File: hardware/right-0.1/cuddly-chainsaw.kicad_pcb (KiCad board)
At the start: 2 copper layers, 181.9 x 100.8 mm, 145 parts, among them J1 USB_C_Receptacle_USB2.0, J2 USB_C_Receptacle_USB2.0, J3 AVR-ISP-6, SW1 Encoder_MX_RGB, SW10 MX_RGB, SW11 MX_RGB, SW12 MX_RGB, SW13 MX_RGB, SW14 MX_RGB, SW15 MX_RGB, SW16 MX_RGB, SW17 MX_RGB, SW18 MX_RGB, SW19 MX_RGB, SW2 MX_RGB, SW20 MX_RGB, SW21 MX_RGB, SW22 MX_RGB, SW23 MX_RGB, SW24 MX_RGB, SW25 MX_RGB, SW26 MX_RGB, SW27 MX_RGB, SW28 MX_RGB, SW29 MX_RGB, SW3 MX_RGB, SW30 MX_RGB, SW31 MX_RGB, SW32 MX_RGB, SW33 MX_RGB, SW34 MX_RGB, SW35 SW_Push, SW36 MX_RGB, SW37 MX_RGB, SW38 MX_RGB, SW39 MX_RGB, SW4 MX_RGB, SW40 MX_RGB, SW41 MX_RGB, SW42 MX_RGB, SW5 MX_RGB, SW6 MX_RGB, SW7 MX_RGB, SW8 MX_RGB, SW9 MX_RGB, U1 USBLC6-2SC6, U2 ATmega32U4-MU, Y1 16MHz

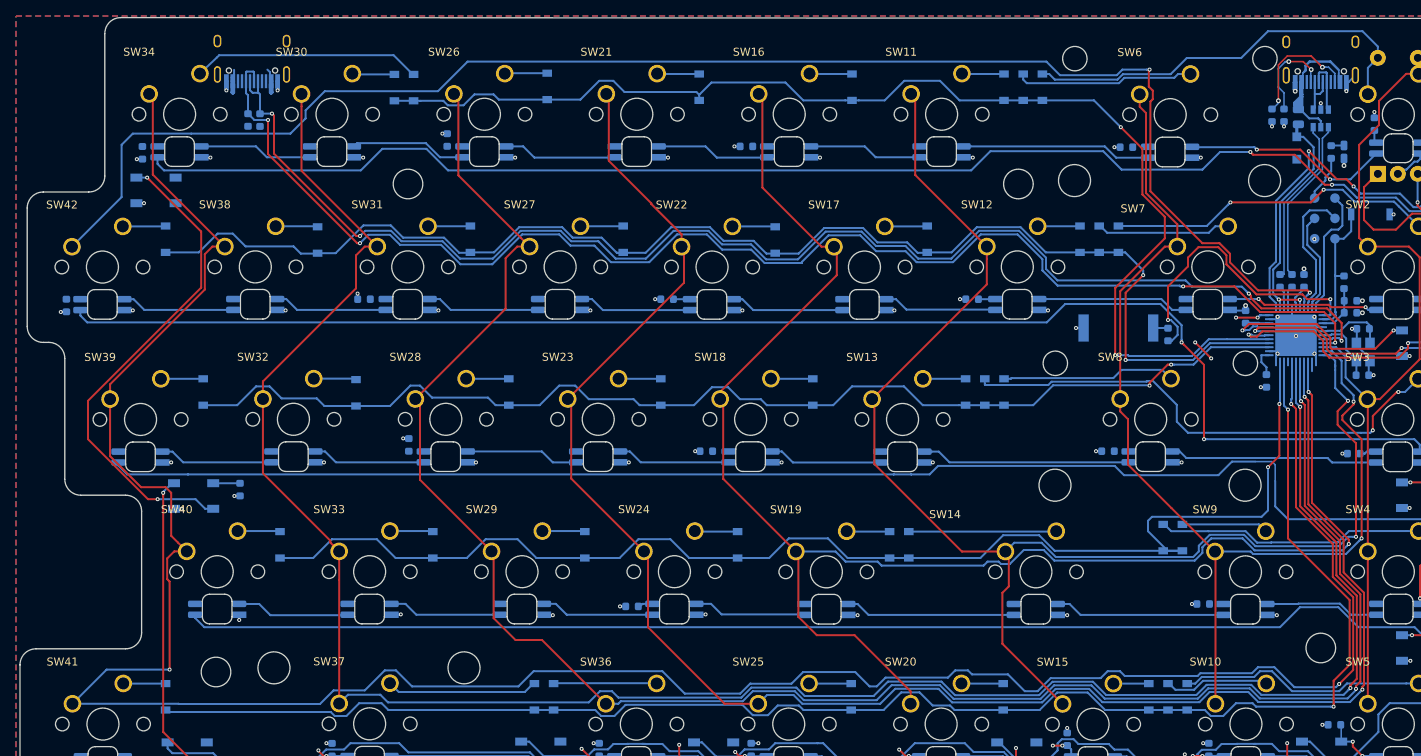
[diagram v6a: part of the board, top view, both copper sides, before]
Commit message: update board with new footprints
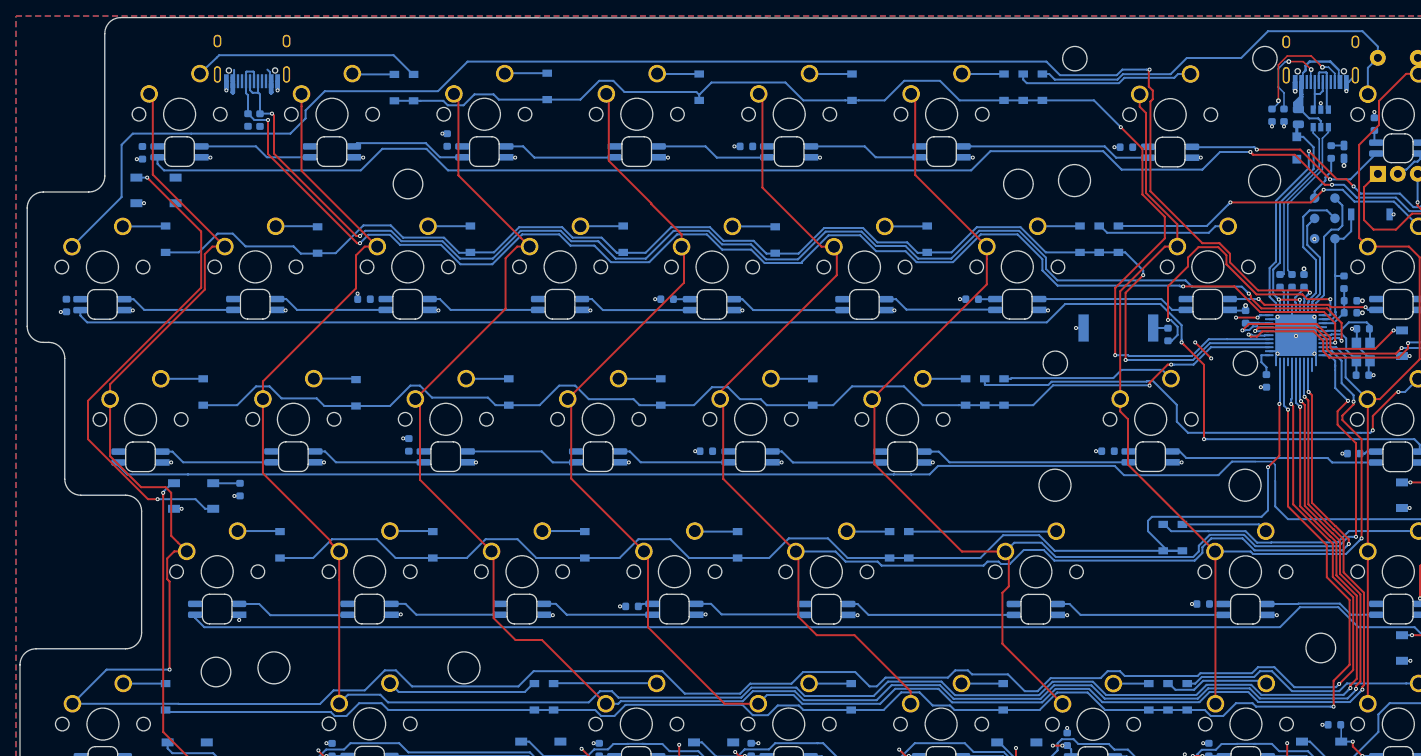
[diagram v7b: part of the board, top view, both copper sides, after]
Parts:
- SW1: footprint josh-buttons-switches:MX_KEYSWITCH_ENCODER_RGB -> josh-keyboard:MX_KEYSWITCH_ENCODER_RGB
